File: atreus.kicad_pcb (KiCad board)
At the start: 2 copper layers, 232 x 90 mm, 91 parts, among them U1 ATmega32U4-AU, Y1 Crystal_GND24_Small

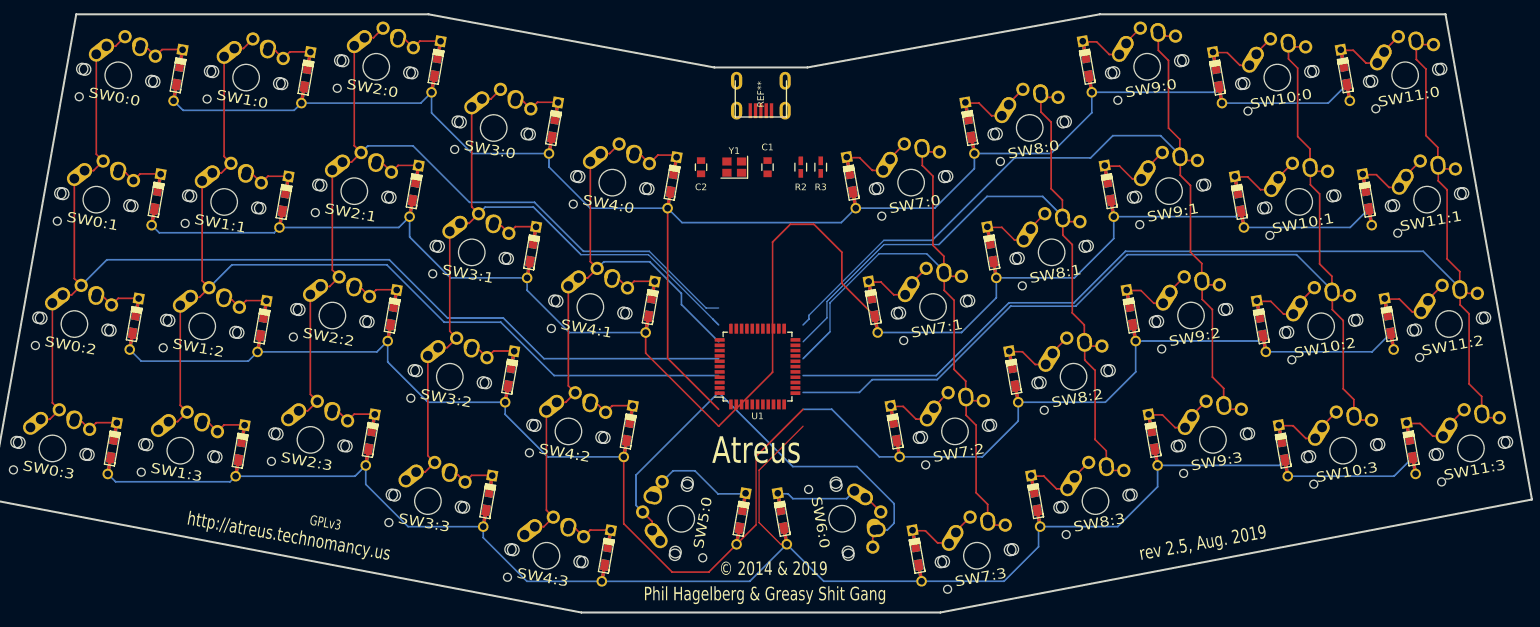
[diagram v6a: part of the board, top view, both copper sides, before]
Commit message: added 0.1uf capacitors.
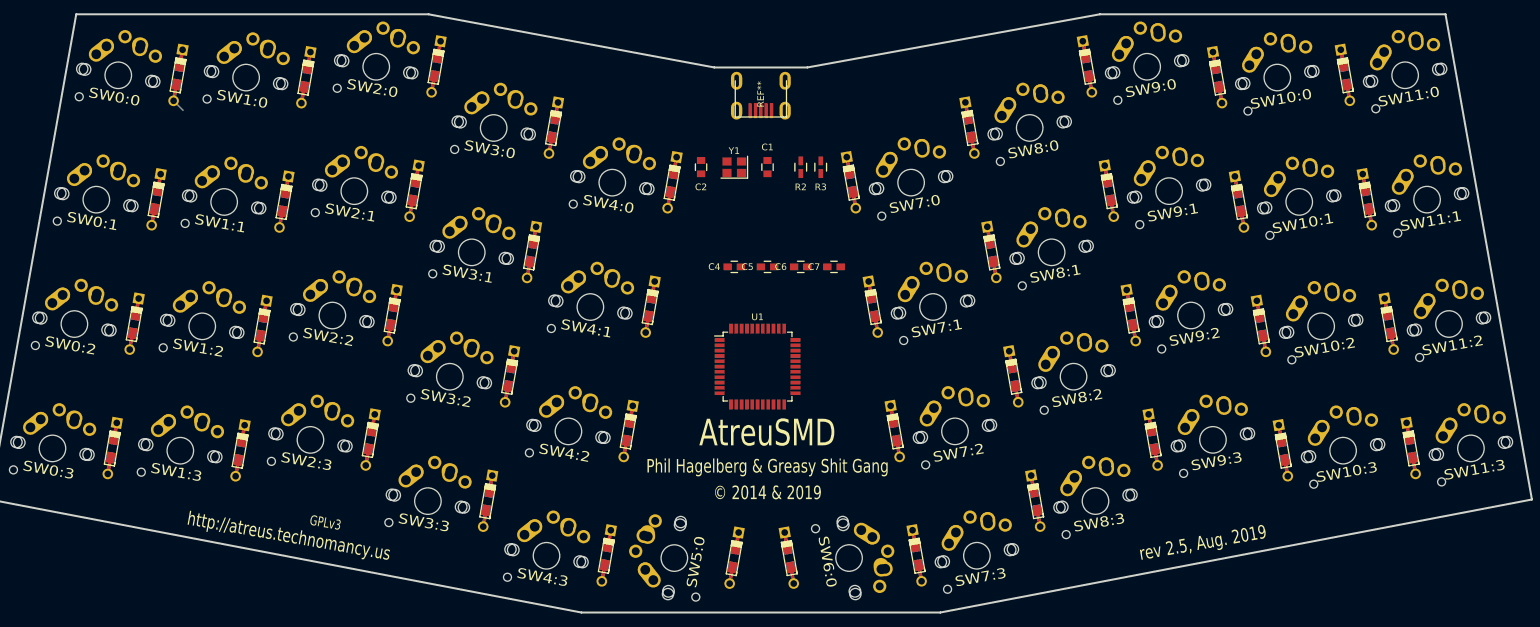
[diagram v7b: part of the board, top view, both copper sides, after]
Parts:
- removed the D2:2 at (131.0, 97.9)
- removed the D2:2 at (137.2, 97.9)
- added C4: 0.1pf, Capacitors_SMD:C_0805, F.Cu at (130.0, 60.0)
- added C5: 0.1pf, Capacitors_SMD:C_0805, F.Cu at (135.0, 60.0)
- added C6: 0.1pf, Capacitors_SMD:C_0805, F.Cu at (140.0, 60.0)
- added C7: 0.1pf, Capacitors_SMD:C_0805, F.Cu at (145.0, 60.0)
- added D2:2: , DIODE, F.Cu at (130.0, 103.8)
- added D2:2: , DIODE, F.Cu at (138.3, 103.8)
- moved SW6:0 6.00 mm to (147.3, 103.8)
- moved SW5:0 6.00 mm to (121.0, 103.8)
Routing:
- net N-row-3: track 248.1 -> 0.00 mm
- net N-row-2: track 246.7 -> 0.00 mm
- net N-row-1: track 246.4 -> 0.00 mm
- net N-row-0: track 235.1 -> 2.02 mm
- net N-col-10: track 178.6 -> 0.00 mm
- net N-col-0: track 166.7 -> 0.00 mm
- net N-col-9: track 160.4 -> 0.00 mm
- net N-col-1: track 148.0 -> 0.00 mm
- net N-col-8: track 139.8 -> 0.00 mm
- net N-col-2: track 127.3 -> 0.00 mm
- net N-col-7: track 122.3 -> 0.00 mm
- net N-col-3: track 106.9 -> 0.00 mm
- net N-col-6: track 101.4 -> 0.00 mm
- net N-col-4: track 87.7 -> 0.00 mm
- net N-col-5: track 69.3 -> 0.00 mm
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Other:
- board text added: "AtreuSMD"
- board text removed: "Atreus"

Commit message: completed the components.
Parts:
- added C3: 1uf, Capacitors_SMD:C_0805, F.Cu at (120.0, 75.0)
- added R1: 10k, Resistors_SMD:R_0805, F.Cu at (123.0, 80.0)
- added R4: 10k, Resistors_SMD:R_0805, F.Cu at (145.0, 70.0)
- C4, C5, C6: value 0.1pf -> 0.1uf
- C7: value 0.1pf -> 10uf
- moved C4 26.0 mm to (123.0, 85.0), turned to 90 degrees
- moved C7 24.2 mm to (123.0, 70.0), turned to 90 degrees
- moved C5 18.0 mm to (145.0, 75.0), turned to 90 degrees
- moved C6 7.07 mm to (135.0, 65.0)
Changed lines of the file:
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@@
    (net 102 +5V)))
 (module Capacitors_SMD:C_0805 (layer F.Cu)
-  (at 130 60 0)
+  (at 120 75 270)
+  (descr "Capacitor SMD 0805, reflow soldering, AVX (see smccp.pdf)")
+  (tags "capacitor 0805")
+  (attr smd)
+  (fp_text
+   reference
+   "C3"
+   (at -3 0 0)
+   (layer F.SilkS)
+   (effects (font (size 1 1) (thickness 0.15))))
+  (fp_text
+   value
+   "1uf"
+   (at 0 -1.75 90)
+   (layer F.Fab)
+   (effects (font (size 1 1) (thickness 0.15))))
+  (fp_line (start -1 -0.62) (end -1 0.62) (layer F.Fab) (width 0.1))
+  (fp_line (start 1 -0.62) (end -1 -0.62) (layer F.Fab) (width 0.1))
+  (fp_line (start 1 0.62) (end 1 -0.62) (layer F.Fab) (width 0.1))
+  (fp_line (start -1 0.62) (end 1 0.62) (layer F.Fab) (width 0.1))
+  (fp_line (start 0.5 0.85) (end -0.5 0.85) (layer F.SilkS) (width 0.12))
+  (fp_line (start -0.5 -0.85) (end 0.5 -0.85) (layer F.SilkS) (width 0.12))
+  (fp_line (start -1.75 0.88) (end 1.75 0.88) (layer F.CrtYd) (width 0.05))
+  (fp_line (start -1.75 0.88) (end -1.75 -0.87) (layer F.CrtYd) (width 0.05))
+  (fp_line (start 1.75 -0.87) (end 1.75 0.88) (layer F.CrtYd) (width 0.05))
+  (fp_line (start 1.75 -0.87) (end -1.75 -0.87) (layer F.CrtYd) (width 0.05))
+  (pad
+   1
+   smd
+   rect
+   (at -1 0 90)
+   (size 1 1.25)
+   (layers F.Cu F.Paste F.Mask)
+   (net 105 GND))
+  (pad
+   2
+   smd
+   rect
+   (at 1 0 90)
+   (size 1 1.25)
+   (layers F.Cu F.Paste F.Mask)
+   (net 106 Net-C3-Pad1)))
+(module Capacitors_SMD:C_0805 (layer F.Cu)
+  (at 123 85 90)
   (descr "Capacitor SMD 0805, reflow soldering, AVX (see smccp.pdf)")
   (tags "capacitor 0805")
@@
   (fp_text
    value
-   "0.1pf"
+   "0.1uf"
    (at 0 -1.75 90)
    (layer F.Fab)
@@
    (net 102 +5V)))
 (module Capacitors_SMD:C_0805 (layer F.Cu)
-  (at 135 60 0)
+  (at 145 75 90)
   (descr "Capacitor SMD 0805, reflow soldering, AVX (see smccp.pdf)")
   (tags "capacitor 0805")
@@
   (fp_text
    value
-   "0.1pf"
+   "0.1uf"
    (at 0 -1.75 90)
    (layer F.Fab)
@@
    (net 102 +5V)))
 (module Capacitors_SMD:C_0805 (layer F.Cu)
-  (at 140 60 0)
+  (at 135 65 0)
   (descr "Capacitor SMD 0805, reflow soldering, AVX (see smccp.pdf)")
   (tags "capacitor 0805")
@@
   (fp_text
    value
-   "0.1pf"
+   "0.1uf"
    (at 0 -1.75 90)
    (layer F.Fab)
@@
    (net 102 +5V)))
 (module Capacitors_SMD:C_0805 (layer F.Cu)
-  (at 145 60 0)
+  (at 123 70 90)
   (descr "Capacitor SMD 0805, reflow soldering, AVX (see smccp.pdf)")
   (tags "capacitor 0805")
@@
   (fp_text
    value
-   "0.1pf"
+   "10uf"
    (at 0 -1.75 90)
    (layer F.Fab)
@@
    (layers F.Cu F.Paste F.Mask)
    (net 102 +5V)))
+(module Resistors_SMD:R_0805 (layer F.Cu)
+  (at 123 80 270)
+  (descr "Resistor SMD 0805, reflow soldering, Vishay (see dcrcw.pdf)")
+  (tags "resistor 0805")
+  (attr smd)
+  (fp_text
+   reference
+   "R1"
+   (at -3 0 0)
+   (layer F.SilkS)
+   (effects (font (size 1 1) (thickness 0.15))))
+  (fp_text
+   value
+   "10k"
+   (at 0 -1.75 90)
+   (layer F.Fab)
+   (effects (font (size 1 1) (thickness 0.15))))
+  (fp_line (start -1 -0.62) (end -1 0.62) (layer F.Fab) (width 0.1))
+  (fp_line (start 1 -0.62) (end -1 -0.62) (layer F.Fab) (width 0.1))
+  (fp_line (start 1 0.62) (end 1 -0.62) (layer F.Fab) (width 0.1))
+  (fp_line (start -1 0.62) (end 1 0.62) (layer F.Fab) (width 0.1))
+  (fp_line (start 0.6 -0.88) (end -0.6 -0.88) (layer F.SilkS) (width 0.12))
+  (fp_line (start -0.6 0.88) (end 0.6 0.88) (layer F.SilkS) (width 0.12))
+  (fp_line (start -1.55 0.9) (end 1.55 0.9) (layer F.CrtYd) (width 0.05))
+  (fp_line (start -1.55 0.9) (end -1.55 -0.9) (layer F.CrtYd) (width 0.05))
+  (fp_line (start 1.55 -0.9) (end 1.55 0.9) (layer F.CrtYd) (width 0.05))
+  (fp_line (start 1.55 -0.9) (end -1.55 -0.9) (layer F.CrtYd) (width 0.05))
+  (pad
+   1
+   smd
+   rect
+   (at -0.95 0 360)
+   (size 0.7 1.3)
+   (layers F.Cu F.Paste F.Mask)
+   (net 102 +5V))
+  (pad
+   2
+   smd
+   rect
+   (at 0.95 0 360)
+   (size 0.7 1.3)
+   (layers F.Cu F.Paste F.Mask)
+   (net 113 Net-R1-Pad2)))
+(module Resistors_SMD:R_0805 (layer F.Cu)
+  (at 145 70 270)
+  (descr "Resistor SMD 0805, reflow soldering, Vishay (see dcrcw.pdf)")
+  (tags "resistor 0805")
+  (attr smd)
+  (fp_text
+   reference
+   "R4"
+   (at -3 0 0)
+   (layer F.SilkS)
+   (effects (font (size 1 1) (thickness 0.15))))
+  (fp_text
+   value
+   "10k"
+   (at 0 -1.75 90)
+   (layer F.Fab)
+   (effects (font (size 1 1) (thickness 0.15))))
+  (fp_line (start -1 -0.62) (end -1 0.62) (layer F.Fab) (width 0.1))
+  (fp_line (start 1 -0.62) (end -1 -0.62) (layer F.Fab) (width 0.1))
+  (fp_line (start 1 0.62) (end 1 -0.62) (layer F.Fab) (width 0.1))
+  (fp_line (start -1 0.62) (end 1 0.62) (layer F.Fab) (width 0.1))
+  (fp_line (start 0.6 -0.88) (end -0.6 -0.88) (layer F.SilkS) (width 0.12))
+  (fp_line (start -0.6 0.88) (end 0.6 0.88) (layer F.SilkS) (width 0.12))
+  (fp_line (start -1.55 0.9) (end 1.55 0.9) (layer F.CrtYd) (width 0.05))
+  (fp_line (start -1.55 0.9) (end -1.55 -0.9) (layer F.CrtYd) (width 0.05))
+  (fp_line (start 1.55 -0.9) (end 1.55 0.9) (layer F.CrtYd) (width 0.05))
+  (fp_line (start 1.55 -0.9) (end -1.55 -0.9) (layer F.CrtYd) (width 0.05))
+  (pad
+   1
+   smd
+   rect
+   (at -0.95 0 360)
+   (size 0.7 1.3)
+   (layers F.Cu F.Paste F.Mask)
+   (net 105 GND))
+  (pad
+   2
+   smd
+   rect
+   (at 0.95 0 360)
+   (size 0.7 1.3)
+   (layers F.Cu F.Paste F.Mask)
+   (net 133 Net-R4-Pad2)))
 (module Molex-0548190589 (layer F.Cu)
   (at 134 32 270)
@@
    (net 1 N-row-0)))
 (module Keebio-Parts:MX-Alps-Choc-1U-NoLED (layer Front)
-  (at 90.50418478725455 57.81745532799191 -10)
+  (at 90.50418478725454 57.81745532799191 -10)
   (fp_text
    reference
@@
    (net 8 N-col-3)))
 (module DIODE (layer Front)
-  (at 99.50418478725455 57.81745532799191 80)
+  (at 99.50418478725454 57.81745532799191 80)
   (attr smd)
   (fp_text
@@
    (net 2 N-row-1)))
 (module Keebio-Parts:MX-Alps-Choc-1U-NoLED (layer Front)
-  (at 237.52398385946222 68.59437213050146 10)
+  (at 237.52398385946222 68.59437213050145 10)
   (fp_text
    reference
@@
    (net 42 N-diode-26)))
 (module DIODE (layer Front)
-  (at 228.52398385946222 68.59437213050146 100)
+  (at 228.52398385946222 68.59437213050145 100)
   (attr smd)
   (fp_text
